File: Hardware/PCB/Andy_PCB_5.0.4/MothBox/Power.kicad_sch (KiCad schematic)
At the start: 50 parts, among them J1 DB141V-2.54-4P, J2 DB141V-2.54-4P, J3 DB141V-2.54-4P, Q1 AP30P30Q, Q10 AP30P30Q, Q2 AO3400A, Q8 AP30P30Q, SW2 KH-6X6X5H-STM, U1 Place Holder voltage regulator, U2 XL4015E1, U3 INA219BIDCNT

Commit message: v5.0.4 schematic and PCB done. Ready for review
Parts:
- removed R40: 4.7K, MothBox_footprints_Library:R_0603_1608Metric, symbol MothBox_Symbol_Library:R_Small
- added R42: 100K, MothBox_footprints_Library:R_0603_1608Metric, symbol MothBox_Symbol_Library:R_Small
- D1, D2, D4: value 6.8V -> 18V; DESCRIPTION BZT52C6V8S -> MM1W18; LCSC_Part C46641604 -> C382948
- Q1, Q10, Q8: footprint 0_easyeda_footprints:PDFN3333-8_L3.1-W3.2-P0.65-LS3.4-BL -> MothBox_footprints_Library:PDFN3333-8_L3.1-W3.2-P0.65-LS3.4-BL
- R29, R30, R39: value 10K -> 4.7K; LCSC_Part C25804 -> C23162
- R38, R41: value 4.7K -> 100K; LCSC_Part C23162 -> C25803
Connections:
- net +12V: now also D4.1 (K), R42.2; no longer D2.1 (K)
- net +24V: now also D2.1 (K), Q8.1 (S), Q8.2 (S), Q8.3 (S), R41.2; no longer D4.1 (K), Q8.5 (D), Q8.6 (D), Q8.7 (D), Q8.8 (D), Q8.9 (D)
- net GND: now also R29.2, R39.2; no longer R38.2, R41.1
- net at Q10.4 (G), R39.1: now also D4.2 (A), R42.1; no longer D2.2 (A)
- net at J3.3 (Pin_3), J3.4 (Pin_4), U1.1 (Vin+): now also Q8.5 (D), Q8.6 (D), Q8.7 (D), Q8.8 (D), Q8.9 (D); no longer Q8.1 (S), Q8.2 (S), Q8.3 (S)
- net at D1.1 (K), F2.1, Q1.1 (S)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: now also R38.2
- net at R38.1: now also D1.2 (A), Q1.4 (G), R29.1; no longer R29.2
- net at R30.2: now also Q2.3 (D); no longer D4.2 (A)
- net at Q8.4 (G): now also D2.2 (A), R30.1, R41.1; no longer Q2.3 (D)
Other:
- note added: "*Use for fine adjustments"
- note added: "*Vout = 1.25 * (1+(Rtop/Rbottom)) 5.416V = 1.25 * (1+(10K/3.0K)) 5.282V = 1.25 * (1+(10K/3.1K)) 5.156V = 1.25 * (1+(10K/3.2K)) 5.078V = 1.25 * (1+(10K/3.3K))"
- note added: "Buck Convertor (Input <9V-36V> PWR to +5.4V)"
- note added: "Up to 4A output at 5.4V"
- note removed: "Buck Convertor (Input <9V-36V> PWR to +5.2V)"
- note removed: "Up to 4A output at 5.2V"
- note removed: "Use for fine adjustments"
- moved on the sheet: C15, C6, C8, D3, E1, F2, J2, Q1, Q2, Q8, R1, R29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

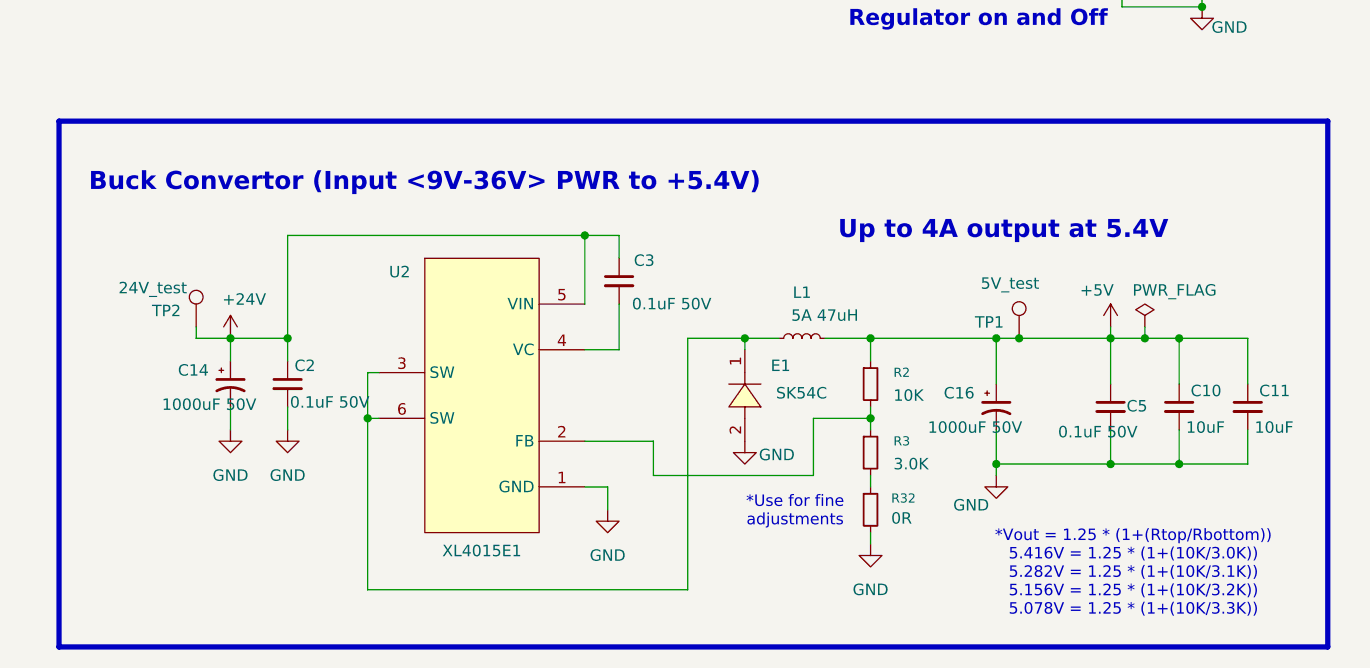
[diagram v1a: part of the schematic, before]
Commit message: version 5.0.4 finished
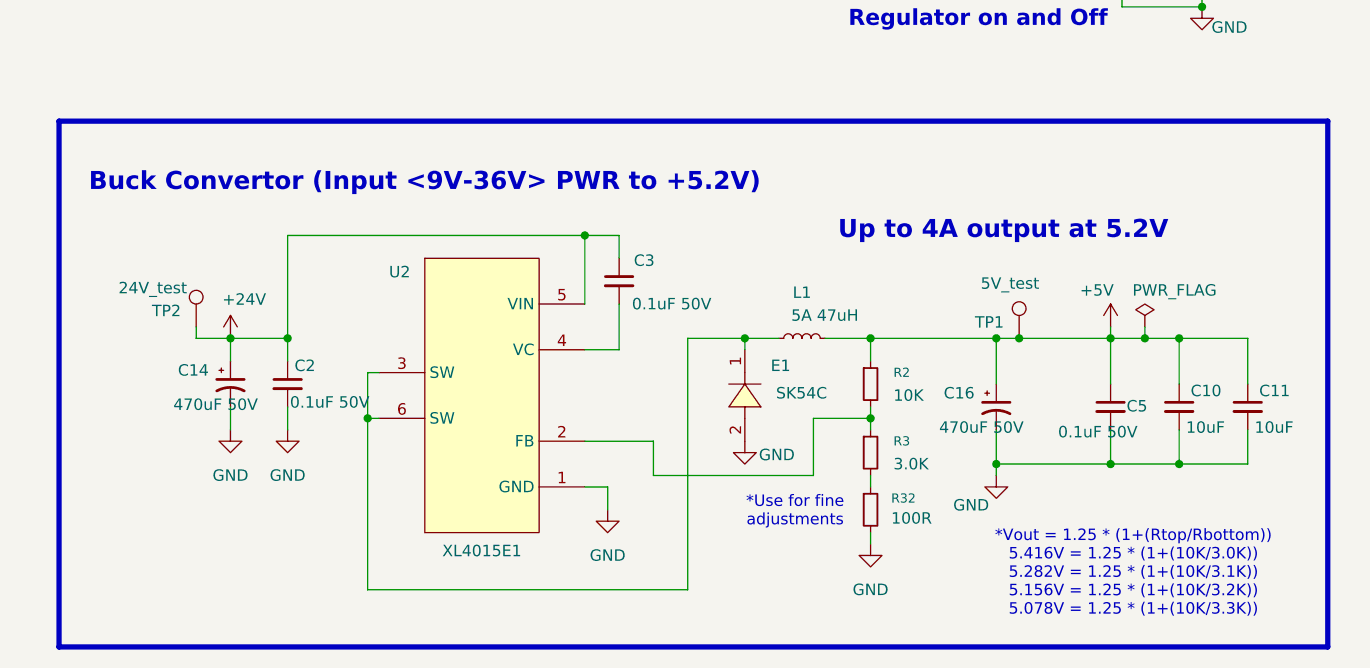
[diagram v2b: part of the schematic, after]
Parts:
- C14, C16: value 1000uF 50V -> 470uF 50V; footprint easyeda2kicad:CAP-TH_BD16.0-P7.50-D1.2-FD -> 0_easyeda_footprints:CAP-SMD_BD12.5-L13.0-W13.0-RD; LCSC_Part C106656 -> C90272
- R32: value 0R -> 100R
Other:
- note added: "Buck Convertor (Input <9V-36V> PWR to +5.2V)"
- note added: "Up to 4A output at 5.2V"
- note removed: "Buck Convertor (Input <9V-36V> PWR to +5.4V)"
- note removed: "Up to 4A output at 5.4V"
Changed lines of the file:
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@@
 		)
 	)
-	(text "Buck Convertor (Input <9V-36V> PWR to +5.4V)"
+	(text "Buck Convertor (Input <9V-36V> PWR to +5.2V)"
 		(exclude_from_sim no)
 		(at 71.12 121.158 0)
@@
 		)
 	)
-	(text "Up to 4A output at 5.4V"
+	(text "Up to 4A output at 5.2V"
 		(exclude_from_sim no)
 		(at 135.382 126.492 0)
@@
 			)
 		)
-		(property "Value" "0R"
+		(property "Value" "100R"
 			(at 122.936 158.4299 0)
 			(effects
@@
 	)
 	(symbol
+		(lib_id "MothBox_Symbol_Library:C_Polarized_Small_US")
+		(at 49.53 143.51 0)
+		(unit 1)
+		(exclude_from_sim no)
+		(in_bom yes)
+		(on_board yes)
+		(dnp no)
+		(property "Reference" "C14"
+			(at 43.688 141.986 0)
+			(effects
+				(font
+					(size 1.27 1.27)
+				)
+				(justify left)
+			)
+		)
+		(property "Value" "470uF 50V"
+			(at 43.18 145.796 0)
+			(effects
+				(font
+					(size 1.27 1.27)
+				)
+				(justify left)
+			)
+		)
+		(property "Footprint" "0_easyeda_footprints:CAP-SMD_BD12.5-L13.0-W13.0-RD"
+			(at 49.53 143.51 0)
+			(effects
+				(font
+					(size 1.27 1.27)
+				)
+				(hide yes)
+			)
+		)
+		(property "Datasheet" ""
+			(at 49.53 143.51 0)
+			(effects
+				(font
+					(size 1.27 1.27)
+				)
+				(hide yes)
+			)
+		)
+		(property "Description" ""
+			(at 49.53 143.51 0)
+			(effects
+				(font
+					(size 1.27 1.27)
+				)
+				(hide yes)
+			)
+		)
+		(property "AVAILABILITY" ""
+			(at 49.53 143.51 0)
+			(effects
+				(font
+					(size 1.27 1.27)
+				)
+				(hide yes)
+			)
+		)
+		(property "DESCRIPTION" ""
+			(at 49.53 143.51 0)
+			(effects
+				(font
+					(size 1.27 1.27)
+				)
+				(hide yes)
+			)
+		)
+		(property "Link" ""
+			(at 49.53 143.51 0)
+			(effects
+				(font
+					(size 1.27 1.27)
+				)
+				(hide yes)
+			)
+		)
+		(property "PACKAGE" ""
+			(at 49.53 143.51 0)
+			(effects
+				(font
+					(size 1.27 1.27)
+				)
+				(hide yes)
+			)
+		)
+		(property "PRICE" ""
+			(at 49.53 143.51 0)
+			(effects
+				(font
+					(size 1.27 1.27)
+				)
+				(hide yes)
+			)
+		)
+		(property "LCSC_Part_No" ""
+			(at 49.53 143.51 0)
+			(effects
+				(font
+					(size 1.27 1.27)
+				)
+				(hide yes)
+			)
+		)
+		(property "Ali_Express_Link" ""
+			(at 49.53 143.51 0)
+			(effects
+				(font
+					(size 1.27 1.27)
+				)
+				(hide yes)
+			)
+		)
+		(property "LCSC_PN" ""
+			(at 49.53 143.51 0)
+			(effects
+				(font
+					(size 1.27 1.27)
+				)
+				(hide yes)
+			)
+		)
+		(property "Sim.Device" ""
+			(at 49.53 143.51 0)
+			(effects
+				(font
+					(size 1.27 1.27)
+				)
+				(hide yes)
+			)
+		)
+		(property "Sim.Pins" ""
+			(at 49.53 143.51 0)
+			(effects
+				(font
+					(size 1.27 1.27)
+				)
+				(hide yes)
+			)
+		)
+		(property "Sim.Type" ""
+			(at 49.53 143.51 0)
+			(effects
+				(font
+					(size 1.27 1.27)
+				)
+				(hide yes)
+			)
+		)
+		(property "LCSC_Part" "C90272"
+			(at 49.53 143.51 0)
+			(effects
+				(font
+					(size 1.27 1.27)
+				)
+				(hide yes)
+			)
+		)
+		(pin "2"
+		)
+		(pin "1"
+		)
+		(instances
+			(project "Mothbox_5.0.4"
+				(path "/9021e528-fc76-4423-a3f3-30f5652071cc/4a573100-9946-48c2-8ae5-35f893607623"
+					(reference "C14")
+					(unit 1)
+				)
+			)
+		)
+	)
+	(symbol
 		(lib_id "MothBox_Symbol_Library:GND")
 		(at 49.53 148.59 0)
@@
 			)
 		)
-		(property "Value" "1000uF 50V"
-			(at 127 148.336 0)
+		(property "Value" "470uF 50V"
+			(at 128.27 148.336 0)
 			(effects
 				(font
@@
 			)
 		)
-		(property "Footprint" "easyeda2kicad:CAP-TH_BD16.0-P7.50-D1.2-FD"
+		(property "Footprint" "0_easyeda_footprints:CAP-SMD_BD12.5-L13.0-W13.0-RD"
 			(at 134.62 146.05 0)
 			(effects
@@
 			)
 		)
-		(property "Datasheet" "https://lcsc.com/product-detail/Aluminum-Electrolytic-Capacitors-Leaded_1000uF-20-50V_C106656.html"
+		(property "Datasheet" ""
 			(at 134.62 146.05 0)
 			(effects
@@
 			)
 		)
-		(property "LCSC_Part" "C106656"
+		(property "LCSC_Part" "C90272"
 			(at 134.62 146.05 0)
 			(effects
@@
 					(unit 1)
 				)
-			)
-		)
-	)
-	(symbol
-		(lib_id "MothBox_Symbol_Library:C_Polarized_Small_US")
-		(at 49.53 143.51 0)
-		(unit 1)
-		(exclude_from_sim no)
-		(in_bom yes)
-		(on_board yes)
-		(dnp no)
-		(property "Reference" "C14"
-			(at 43.688 141.986 0)
-			(effects
-				(font
-					(size 1.27 1.27)
-				)
-				(justify left)
-			)
-		)
-		(property "Value" "1000uF 50V"
-			(at 41.91 145.796 0)
-			(effects
-				(font
-					(size 1.27 1.27)
-				)
-				(justify left)
-			)
-		)
-		(property "Footprint" "easyeda2kicad:CAP-TH_BD16.0-P7.50-D1.2-FD"
-			(at 49.53 143.51 0)
-			(effects
-				(font
-					(size 1.27 1.27)
-				)
-				(hide yes)
-			)
-		)
-		(property "Datasheet" "~"
-			(at 49.53 143.51 0)
-			(effects
-				(font
-					(size 1.27 1.27)
-				)
-				(hide yes)
-			)
-		)
-		(property "Description" "Polarized capacitor, small US symbol"
-			(at 49.53 143.51 0)
-			(effects
-				(font
-					(size 1.27 1.27)
-				)
-				(hide yes)
-			)
-		)
-		(property "AVAILABILITY" ""
-			(at 49.53 143.51 0)
-			(effects
-				(font
-					(size 1.27 1.27)
-				)
-				(hide yes)
-			)
-		)
-		(property "DESCRIPTION" ""
-			(at 49.53 143.51 0)
-			(effects
-				(font
-					(size 1.27 1.27)
-				)
-				(hide yes)
-			)
-		)
-		(property "Link" ""
-			(at 49.53 143.51 0)
-			(effects
-				(font
-					(size 1.27 1.27)
-				)
-				(hide yes)
-			)
-		)
-		(property "PACKAGE" ""
-			(at 49.53 143.51 0)
-			(effects
-				(font
-					(size 1.27 1.27)
-				)
-				(hide yes)
-			)
-		)
-		(property "PRICE" ""
-			(at 49.53 143.51 0)
-			(effects
-				(font
-					(size 1.27 1.27)
-				)
-				(hide yes)
-			)
-		)
-		(property "LCSC_Part_No" ""
-			(at 49.53 143.51 0)
-			(effects
-				(font
-					(size 1.27 1.27)
-				)
-				(hide yes)
-			)
-		)
-		(property "Ali_Express_Link" ""
-			(at 49.53 143.51 0)
-			(effects
-				(font
-					(size 1.27 1.27)
-				)
-				(hide yes)
-			)
-		)
-		(property "LCSC_PN" ""
-			(at 49.53 143.51 0)
-			(effects
-				(font
-					(size 1.27 1.27)
-				)
-				(hide yes)
-			)
-		)
-		(property "Sim.Device" ""
-			(at 49.53 143.51 0)
-			(effects
-				(font
-					(size 1.27 1.27)
-				)
-				(hide yes)
-			)
-		)
-		(property "Sim.Pins" ""
-			(at 49.53 143.51 0)
-			(effects
-				(font
-					(size 1.27 1.27)
-				)
-				(hide yes)
-			)
-		)
-		(property "Sim.Type" ""
-			(at 49.53 143.51 0)
-			(effects
-				(font
-					(size 1.27 1.27)
-				)
-				(hide yes)
-			)
-		)
-		(property "LCSC_Part" "C106656"
-			(at 49.53 143.51 0)
-			(effects
-				(font
-					(size 1.27 1.27)
-				)
-				(hide yes)
-			)
-		)
-		(pin "2"
-		)
-		(pin "1"
-		)
-		(instances
-			(project "MothBox5.0.2"
-				(path "/9021e528-fc76-4423-a3f3-30f5652071cc/4a573100-9946-48c2-8ae5-35f893607623"
-					(reference "C14")
-					(unit 1)
-				)

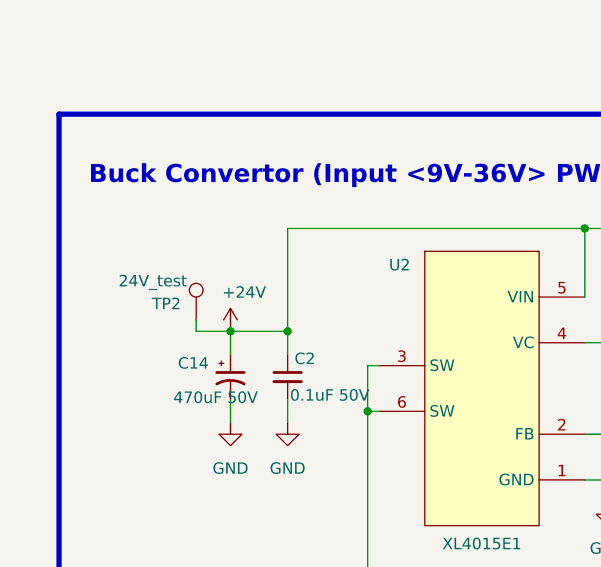
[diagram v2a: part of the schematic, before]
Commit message: renamed 24v areas to be actually 9-36v areas
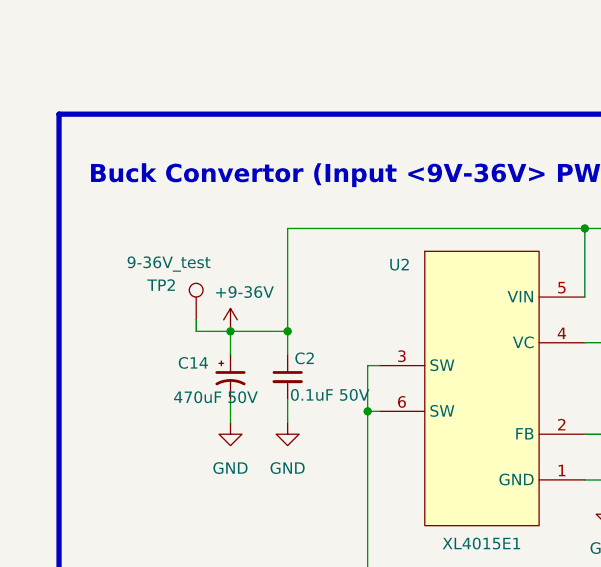
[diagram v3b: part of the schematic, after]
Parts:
- TP2: value 24V_test -> 9-36V_test
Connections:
- net +24V: no longer C14.1, C2.1, C3.1, TP2.1, U2.5 (VIN)
- new net +9-36V: C14.1, C2.1, C3.1, TP2.1, U2.5 (VIN)
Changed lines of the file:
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@@
 		(dnp no)
 		(property "Reference" "TP2"
-			(at 42.418 135.382 0)
-			(effects
-				(font
-					(size 1.27 1.27)
-				)
-			)
-		)
-		(property "Value" "24V_test"
-			(at 40.894 132.842 0)
+			(at 41.91 133.35 0)
+			(effects
+				(font
+					(size 1.27 1.27)
+				)
+			)
+		)
+		(property "Value" "9-36V_test"
+			(at 42.672 130.81 0)
 			(effects
 				(font
@@
 			)
 		)
-		(property "Value" "+24V"
+		(property "Value" "+9-36V"
 			(at 51.054 134.112 0)
 			(effects

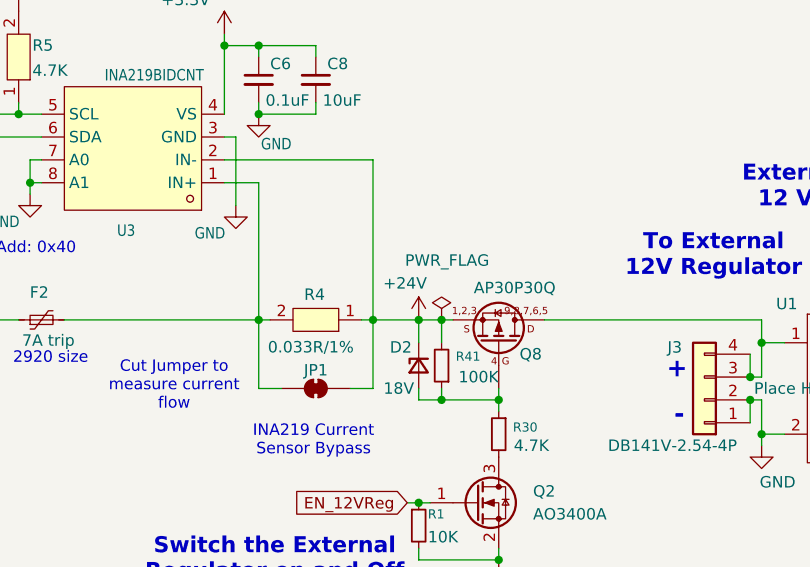
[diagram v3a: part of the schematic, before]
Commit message: Change holes from m2.5 to m3 and fully changed 24 net to 9-36v net
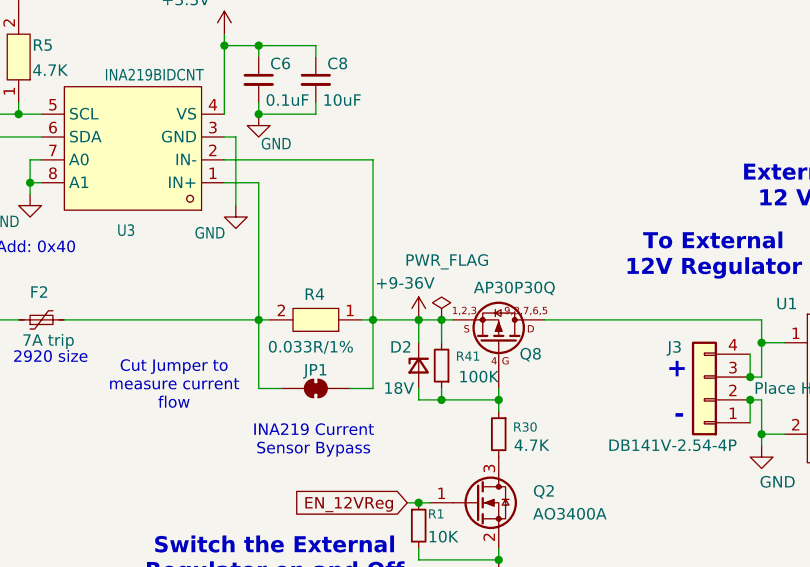
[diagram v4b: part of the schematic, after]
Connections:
- net +24V is gone; now on net +9-36V: D2.1 (K), JP1.2 (B), Q8.1 (S), Q8.2 (S), Q8.3 (S), R4.1, R41.2, U3.2 (IN-)
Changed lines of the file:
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@@
 			)
 		)
-		(property "Value" "+24V"
+		(property "Value" "+9-36V"
 			(at 147.066 70.866 0)
 			(effects
